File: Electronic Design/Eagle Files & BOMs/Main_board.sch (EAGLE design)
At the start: 52 parts, among them IC2 ATMEGA328-PU, IC3 LM2576S, Q1 BSS192P, Q2 FQD7P20, X1 16MHz

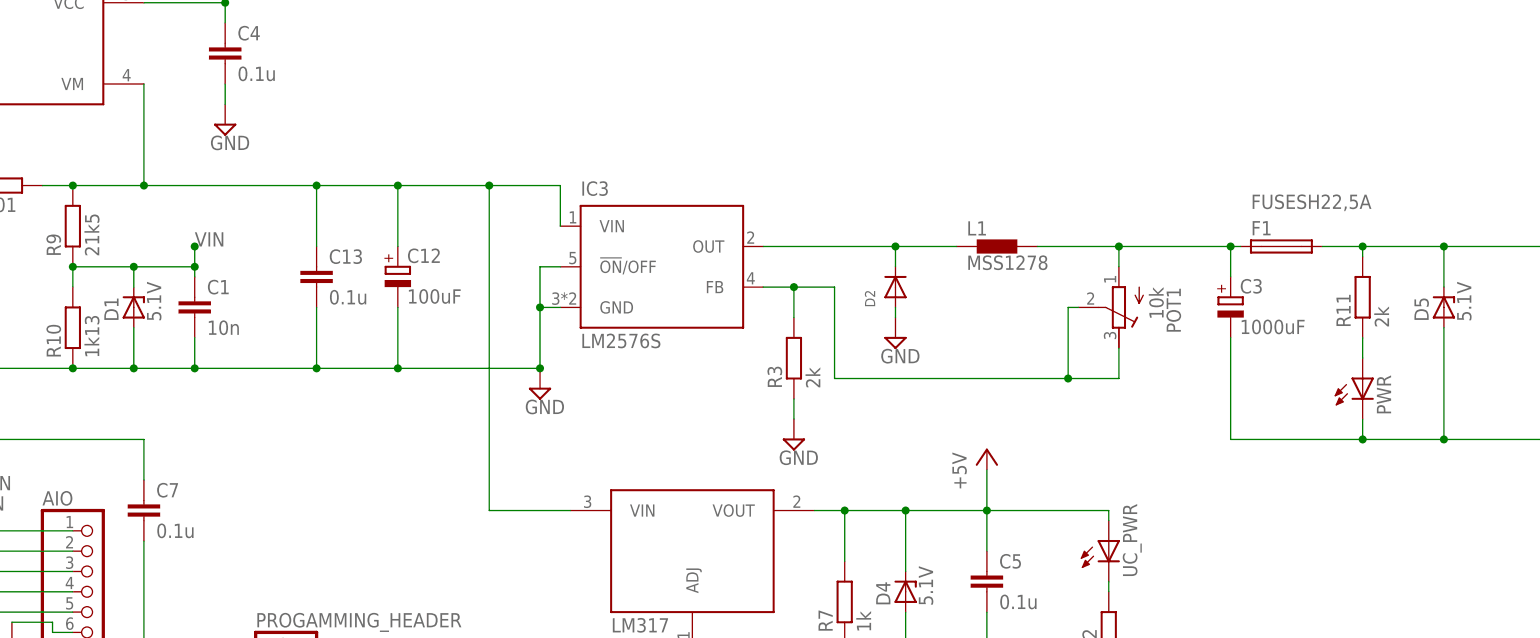
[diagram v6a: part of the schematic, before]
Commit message: replacing homemade buck converter with premade board
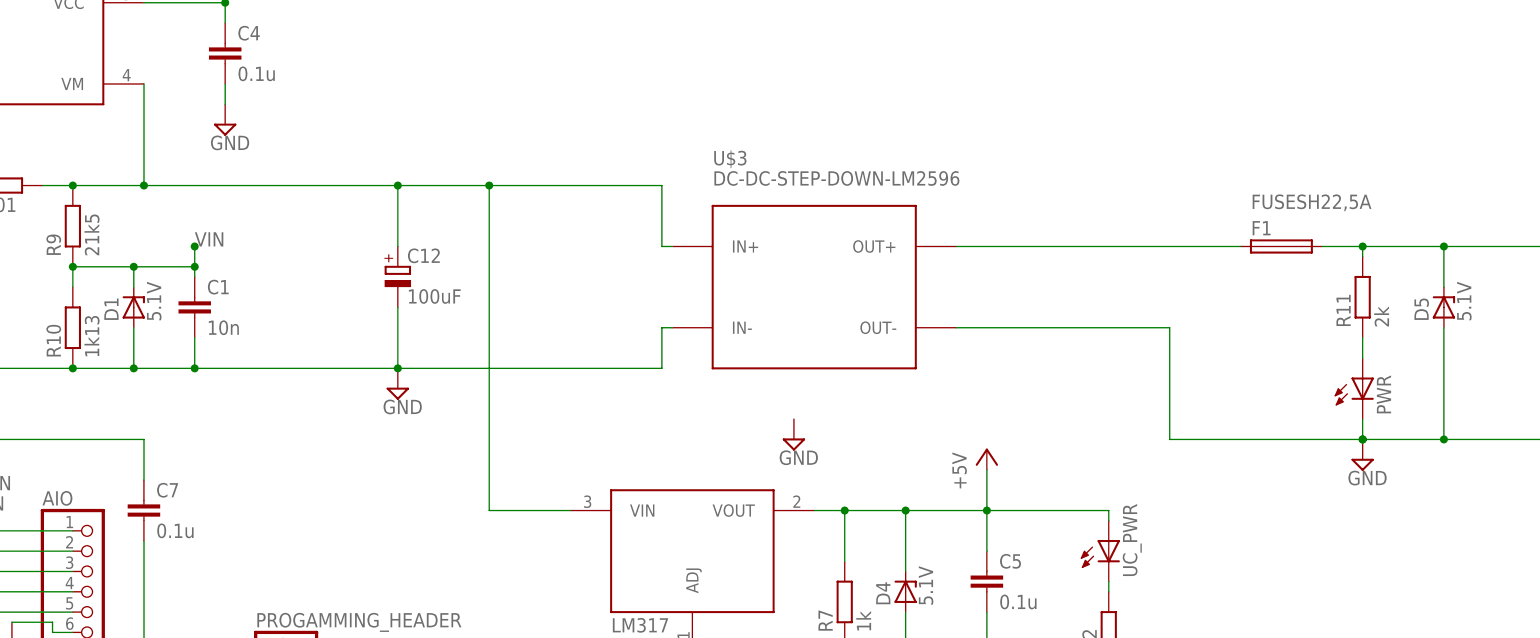
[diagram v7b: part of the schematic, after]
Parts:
- removed C13: 0.1u, resistor:C-EUC1206K
- removed C3: 1000uF, resistor:CPOL-EUE3.5-10
- removed D2: (no value), adafruit:DIODESMA
- removed IC3: LM2576S, Samson:LM2576S
- removed L1: MSS1278, Samson:MSS1278
- removed POT1: 10k, resistor:R-TRIMM3296W
- removed R3: 2k, resistor:R-EU_R1206
- added U$3: DC-DC-STEP-DOWN-LM2596, diy-modules:DC-DC-STEP-DOWN-LM2596
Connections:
- removed net BUCK_FEEDBACK: IC3.FB, POT1.E, POT1.S, R3.2
- removed net BUCK_OUTPUT: D2.C, IC3.OUT, L1.1
- net GND: now also U$3.IN-, U$3.OUT-; no longer C13.2, C3.-, D2.A, IC3.!ON!/OFF, IC3.GND, R3.1
- net VIN_CURRENT_MEASURED: now also U$3.IN+; no longer C13.1, IC3.VIN
- net VOUT_PREFUSE: now also U$3.OUT+; no longer C3.+, L1.2, POT1.A
